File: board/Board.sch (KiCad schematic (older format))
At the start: 56 parts, among them J1 CONN_02X10, J10 CONN_01X03, J11 CONN_01X03, J12 CONN_01X02, J13 CONN_02X09, J14 CONN_02X04, J2 CONN_01X03, J3 CONN_01X03, J4 CONN_01X03, J5 CONN_01X03, J6 CONN_01X03, J7 CONN_01X03, J8 CONN_01X03, J9 CONN_01X03, SW1 SW_Push, SW2 SW_SPDT, SW3 SW_SPDT, U1 STM32F410RBTx, U2 LF33ABDT-TR, U3 ICM-20689, Y1 25 MHz, Y2 32.768 KHz

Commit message: uart signal inverter; battery measurement
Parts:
- removed C3, C4: 1.5pF, Capacitors_SMD:C_0805_HandSoldering, symbol C
- removed R4, R5: 0, Resistors_SMD:R_0805_HandSoldering, symbol R
- removed SW2, SW3: SW_SPDT, Pin_Headers:Pin_Header_Straight_1x03_Pitch2.54mm, symbol SW_SPDT
- removed Y2: 32.768 KHz, Crystals:Crystal_SMD_5032-2pin_5.0x3.2mm_HandSoldering, symbol Crystal
- added J?: CONN_01X01, symbol CONN_01X01
- added J?: GS2, Connectors:GS2, symbol GS2
- added J? (x2): GS3, Connectors:GS3, symbol GS3
- added R?: 62K, symbol R
- added R?: 22K, symbol R
- added U4: SN74LVC1G04, TO_SOT_Packages_SMD:SOT-23-5_HandSoldering, symbol SN74LVC1G04
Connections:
- net labels added: +BATT, BATT_ADC
- net labels removed: +12V
- wire segments 210 -> 206
- no-connect marks 19 -> 20
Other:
- moved on the sheet: J11

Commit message: inverter gate is now optional
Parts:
- added J16: GS3, Connectors:GS3, symbol GS3
- gave numbers to parts that had none: 6
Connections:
- wire segments 206 -> 210
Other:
- moved on the sheet: J11, U4

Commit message: ?
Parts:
- J15, J16, J17: footprint Connectors:GS3 -> Connect:GS3
- J18: footprint Connectors:GS2 -> Connect:GS2
- J19: footprint (none) -> Pin_Headers:Pin_Header_Straight_1x01_Pitch2.54mm
- R4, R5: footprint (none) -> Resistors_SMD:R_0805_HandSoldering
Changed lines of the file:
@@
 F 0 "R4" V 15080 1250 50  0000 C CNN
 F 1 "62K" V 15000 1250 50  0000 C CNN
-F 2 "" V 14930 1250 50  0001 C CNN
+F 2 "Resistors_SMD:R_0805_HandSoldering" V 14930 1250 50  0001 C CNN
 F 3 "" H 15000 1250 50  0001 C CNN
 	1    15000 1250
@@
 F 0 "R5" V 15080 1650 50  0000 C CNN
 F 1 "22K" V 15000 1650 50  0000 C CNN
-F 2 "" V 14930 1650 50  0001 C CNN
+F 2 "Resistors_SMD:R_0805_HandSoldering" V 14930 1650 50  0001 C CNN
 F 3 "" H 15000 1650 50  0001 C CNN
 	1    15000 1650
@@
 F 0 "J19" H 15350 1050 50  0000 C CNN
 F 1 "CONN_01X01" V 15450 950 50  0000 C CNN
-F 2 "" H 15350 950 50  0001 C CNN
+F 2 "Pin_Headers:Pin_Header_Straight_1x01_Pitch2.54mm" H 15350 950 50  0001 C CNN
 F 3 "" H 15350 950 50  0001 C CNN
 	1    15350 950
@@
 F 0 "J18" V 14800 1100 50  0000 C CNN
 F 1 "GS2" V 14800 801 50  0000 C CNN
-F 2 "Connectors:GS2" V 14774 950 50  0001 C CNN
+F 2 "Connect:GS2" V 14774 950 50  0001 C CNN
 F 3 "" H 14700 950 50  0001 C CNN
 	1    14700 950
@@
 F 0 "J15" H 1200 2600 50  0000 C CNN
 F 1 "GS3" H 1200 2201 50  0000 C CNN
-F 2 "Connectors:GS3" V 1238 2326 50  0001 C CNN
+F 2 "Connect:GS3" V 1238 2326 50  0001 C CNN
 F 3 "" H 1150 2400 50  0001 C CNN
 	1    1150 2400
@@
 F 0 "J17" H 10050 4050 50  0000 C CNN
 F 1 "GS3" H 10050 3651 50  0000 C CNN
-F 2 "Connectors:GS3" V 10088 3776 50  0001 C CNN
+F 2 "Connect:GS3" V 10088 3776 50  0001 C CNN
 F 3 "" H 10000 3850 50  0001 C CNN
 	1    10000 3850
@@
 F 0 "J16" H 9600 9250 50  0000 C CNN
 F 1 "GS3" H 9600 8851 50  0000 C CNN
-F 2 "Connectors:GS3" V 9638 8976 50  0001 C CNN
+F 2 "Connect:GS3" V 9638 8976 50  0001 C CNN
 F 3 "" H 9550 9050 50  0001 C CNN
 	1    9550 9050

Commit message: pcb rev2, work in progress
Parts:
- removed J14: CONN_02X04, Pin_Headers:Pin_Header_Straight_2x04_Pitch2.54mm, symbol CONN_02X04
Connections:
- net labels removed: NRF24_CE, NRF24_SPI_CS, NRF24_SPI_MISO, NRF24_SPI_MOSI, NRF24_SPI_SCK
- wire segments 210 -> 196
- no-connect marks 20 -> 24
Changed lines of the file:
@@
 Text GLabel 6150 8350 0    60   Input ~ 0
 PWM_INPUT_4
-$Comp
-L CONN_02X04 J14
-U 1 1 58D8CF93
-P 13500 5750
-F 0 "J14" H 13500 6000 50  0000 C CNN
-F 1 "CONN_02X04" H 13500 5500 50  0000 C CNN
-F 2 "Pin_Headers:Pin_Header_Straight_2x04_Pitch2.54mm" H 13500 4550 50  0001 C CNN
-F 3 "" H 13500 4550 50  0001 C CNN
-	1    13500 5750
-	1    0    0    -1
-$EndComp
-$Comp
-L GND #PWR031
-U 1 1 58D8E88C
-P 13150 6050
-F 0 "#PWR031" H 13150 5800 50  0001 C CNN
-F 1 "GND" H 13150 5900 50  0000 C CNN
-F 2 "" H 13150 6050 50  0001 C CNN
-F 3 "" H 13150 6050 50  0001 C CNN
-	1    13150 6050
-	1    0    0    -1
-$EndComp
-$Comp
-L VCC #PWR032
-U 1 1 58D8FC31
-P 14050 5200
-F 0 "#PWR032" H 14050 5050 50  0001 C CNN
-F 1 "VCC" H 14050 5350 50  0000 C CNN
-F 2 "" H 14050 5200 50  0001 C CNN
-F 3 "" H 14050 5200 50  0001 C CNN
-	1    14050 5200
-	1    0    0    -1
-$EndComp
-NoConn ~ 13750 5900
-Text GLabel 12950 5700 0    60   Input ~ 0
-NRF24_CE
-Text GLabel 14050 5700 2    60   Input ~ 0
-NRF24_SPI_CS
-Text GLabel 11900 5800 0    60   Input ~ 0
-NRF24_SPI_SCK
-Text GLabel 14800 5800 2    60   Input ~ 0
-NRF24_SPI_MOSI
-Text GLabel 12950 5900 0    60   Input ~ 0
-NRF24_SPI_MISO
-Text GLabel 8600 5150 2    60   Input ~ 0
-NRF24_SPI_MOSI
-Text GLabel 9400 5050 2    60   Input ~ 0
-NRF24_SPI_MISO
-Text GLabel 8600 4950 2    60   Input ~ 0
-NRF24_SPI_SCK
-Text GLabel 9400 4850 2    60   Input ~ 0
-NRF24_SPI_CS
-Text GLabel 2450 4250 0    60   Input ~ 0
-NRF24_CE
 Text GLabel 9400 2350 2    60   Input ~ 0
 ICM_SPI_CS
@@
 $EndComp
 $Comp
-L GND #PWR033
+L GND #PWR031
 U 1 1 58DA392C
 P 13700 1800
-F 0 "#PWR033" H 13700 1550 50  0001 C CNN
+F 0 "#PWR031" H 13700 1550 50  0001 C CNN
 F 1 "GND" H 13700 1650 50  0000 C CNN
 F 2 "" H 13700 1800 50  0001 C CNN
@@
 $EndComp
 $Comp
-L GND #PWR034
+L GND #PWR032
 U 1 1 58DA6641
 P 1500 4750
-F 0 "#PWR034" H 1500 4500 50  0001 C CNN
+F 0 "#PWR032" H 1500 4500 50  0001 C CNN
 F 1 "GND" H 1500 4600 50  0000 C CNN
 F 2 "" H 1500 4750 50  0001 C CNN
@@
 I2C_SCL
 $Comp
-L GND #PWR035
+L GND #PWR033
 U 1 1 58D99A32
 P 10300 9400
-F 0 "#PWR035" H 10300 9150 50  0001 C CNN
+F 0 "#PWR033" H 10300 9150 50  0001 C CNN
 F 1 "GND" H 10300 9250 50  0000 C CNN
 F 2 "" H 10300 9400 50  0001 C CNN
@@
 $EndComp
 $Comp
-L VCC #PWR036
+L VCC #PWR034
 U 1 1 58D9B26E
 P 9000 6250
-F 0 "#PWR036" H 9000 6100 50  0001 C CNN
+F 0 "#PWR034" H 9000 6100 50  0001 C CNN
 F 1 "VCC" H 9000 6400 50  0000 C CNN
 F 2 "" H 9000 6250 50  0001 C CNN
@@
 PB5
 $Comp
-L GND #PWR037
+L GND #PWR035
 U 1 1 58DAF3FA
 P 12050 7900
-F 0 "#PWR037" H 12050 7650 50  0001 C CNN
+F 0 "#PWR035" H 12050 7650 50  0001 C CNN
 F 1 "GND" H 12050 7750 50  0000 C CNN
 F 2 "" H 12050 7900 50  0001 C CNN
@@
 $EndComp
 $Comp
-L PWR_FLAG #FLG038
+L PWR_FLAG #FLG036
 U 1 1 58DB2A85
 P 11150 1500
-F 0 "#FLG038" H 11150 1575 50  0001 C CNN
+F 0 "#FLG036" H 11150 1575 50  0001 C CNN
 F 1 "PWR_FLAG" H 10950 1650 50  0000 C CNN
 F 2 "" H 11150 1500 50  0001 C CNN
@@
 $EndComp
 $Comp
-L PWR_FLAG #FLG039
+L PWR_FLAG #FLG037
 U 1 1 58DB1674
 P 11250 1000
-F 0 "#FLG039" H 11250 1075 50  0001 C CNN
+F 0 "#FLG037" H 11250 1075 50  0001 C CNN
 F 1 "PWR_FLAG" H 11250 1150 50  0000 C CNN
 F 2 "" H 11250 1000 50  0001 C CNN
@@
 $EndComp
 $Comp
-L GND #PWR040
+L GND #PWR038
 U 1 1 58DB0976
 P 6550 8900
-F 0 "#PWR040" H 6550 8650 50  0001 C CNN
+F 0 "#PWR038" H 6550 8650 50  0001 C CNN
 F 1 "GND" H 6550 8750 50  0000 C CNN
 F 2 "" H 6550 8900 50  0001 C CNN
@@
 $EndComp
 $Comp
-L VCC #PWR041
+L VCC #PWR039
 U 1 1 58F60FBC
 P 8400 9250
-F 0 "#PWR041" H 8400 9100 50  0001 C CNN
+F 0 "#PWR039" H 8400 9100 50  0001 C CNN
 F 1 "VCC" H 8400 9400 50  0000 C CNN
 F 2 "" H 8400 9250 50  0001 C CNN
@@
 $EndComp
 $Comp
-L GND #PWR042
+L GND #PWR040
 U 1 1 58F61042
 P 8400 9850
-F 0 "#PWR042" H 8400 9600 50  0001 C CNN
+F 0 "#PWR040" H 8400 9600 50  0001 C CNN
 F 1 "GND" H 8400 9700 50  0000 C CNN
 F 2 "" H 8400 9850 50  0001 C CNN
@@
 $EndComp
 $Comp
-L GND #PWR043
+L GND #PWR041
 U 1 1 58F6AF97
 P 15000 1900
-F 0 "#PWR043" H 15000 1650 50  0001 C CNN
+F 0 "#PWR041" H 15000 1650 50  0001 C CNN
 F 1 "GND" H 15000 1750 50  0000 C CNN
 F 2 "" H 15000 1900 50  0001 C CNN
@@
 $EndComp
 $Comp
-L +BATT #PWR044
+L +BATT #PWR042
 U 1 1 58F72A6D
 P 11550 1000
-F 0 "#PWR044" H 11550 850 50  0001 C CNN
+F 0 "#PWR042" H 11550 850 50  0001 C CNN
 F 1 "+BATT" H 11550 1140 50  0000 C CNN
 F 2 "" H 11550 1000 50  0001 C CNN
@@
 $EndComp
 $Comp
-L +BATT #PWR045
+L +BATT #PWR043
 U 1 1 58F73262
 P 14400 800
-F 0 "#PWR045" H 14400 650 50  0001 C CNN
+F 0 "#PWR043" H 14400 650 50  0001 C CNN
 F 1 "+BATT" H 14400 940 50  0000 C CNN
 F 2 "" H 14400 800 50  0001 C CNN
@@
 Wire Wire Line
 	6700 6900 6550 6900
-Wire Wire Line
-	13750 5600 14050 5600
-Wire Wire Line
-	14050 5600 14050 5200
-Wire Wire Line
-	13250 5600 13150 5600
-Wire Wire Line
-	13150 5600 13150 6050
-Wire Wire Line
-	13250 5700 12950 5700
-Wire Wire Line
-	13750 5700 14050 5700
-Wire Wire Line
-	11900 5800 13250 5800
-Wire Wire Line
-	13750 5800 14800 5800
-Wire Wire Line
-	13250 5900 12950 5900
-Wire Wire Line
-	8200 5150 8600 5150
-Wire Wire Line
-	9400 5050 8200 5050
-Wire Wire Line
-	8600 4950 8200 4950
-Wire Wire Line
-	9400 4850 8200 4850
-Wire Wire Line
-	2450 4250 2800 4250
 Wire Wire Line
 	8200 2350 9400 2350
@@
 Wire Wire Line
 	9050 9150 9400 9150
+NoConn ~ 2800 4250
+NoConn ~ 8200 4850
+NoConn ~ 8200 4950
+NoConn ~ 8200 5050
+NoConn ~ 8200 5150
 $EndSCHEMATC

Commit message: removed GPIO headers
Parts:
- removed J13: CONN_02X09, Pin_Headers:Pin_Header_Straight_2x09_Pitch2.54mm, symbol CONN_02X09
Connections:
- net labels removed: PA12, PB11, PB5, PC1, PC11, PC12, PC13, PC2, PC3, PC7, PC8, PC9
- wire segments 196 -> 183
- no-connect marks 24 -> 31
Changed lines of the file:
@@
 	1    0    0    -1
 $EndComp
-Text GLabel 8500 4750 2    60   Input ~ 0
-PB11
-Text GLabel 11100 7300 0    60   Input ~ 0
-PB11
-Text GLabel 2800 3750 0    60   Input ~ 0
-PC1
-Text GLabel 2550 3850 0    60   Input ~ 0
-PC2
-Text GLabel 2800 3950 0    60   Input ~ 0
-PC3
-Text GLabel 11100 7500 0    60   Input ~ 0
-PC1
-Text GLabel 11400 7600 0    60   Input ~ 0
-PC2
-Text GLabel 11100 7700 0    60   Input ~ 0
-PC3
-Text GLabel 2800 4350 0    60   Input ~ 0
-PC7
-Text GLabel 2500 4450 0    60   Input ~ 0
-PC8
-Text GLabel 2800 4550 0    60   Input ~ 0
-PC9
-Text GLabel 2800 4750 0    60   Input ~ 0
-PC11
-Text GLabel 2500 4850 0    60   Input ~ 0
-PC12
-Text GLabel 2800 4950 0    60   Input ~ 0
-PC13
-Text GLabel 11400 7800 0    60   Input ~ 0
-PC7
-Text GLabel 11900 7000 2    60   Input ~ 0
-PC8
-Text GLabel 12250 7300 2    60   Input ~ 0
-PC11
-Text GLabel 12250 7100 2    60   Input ~ 0
-PC9
-Text GLabel 11900 7400 2    60   Input ~ 0
-PC12
-Text GLabel 12250 7500 2    60   Input ~ 0
-PC13
-Text GLabel 8200 4150 2    60   Input ~ 0
-PB5
-Text GLabel 8200 3150 2    60   Input ~ 0
-PA12
-Text GLabel 12250 7700 2    60   Input ~ 0
-PA12
-Text GLabel 11900 7600 2    60   Input ~ 0
-PB5
-$Comp
-L GND #PWR035
-U 1 1 58DAF3FA
-P 12050 7900
-F 0 "#PWR035" H 12050 7650 50  0001 C CNN
-F 1 "GND" H 12050 7750 50  0000 C CNN
-F 2 "" H 12050 7900 50  0001 C CNN
-F 3 "" H 12050 7900 50  0001 C CNN
-	1    12050 7900
-	1    0    0    -1
-$EndComp
-$Comp
-L PWR_FLAG #FLG036
+$Comp
+L PWR_FLAG #FLG035
 U 1 1 58DB2A85
 P 11150 1500
-F 0 "#FLG036" H 11150 1575 50  0001 C CNN
+F 0 "#FLG035" H 11150 1575 50  0001 C CNN
 F 1 "PWR_FLAG" H 10950 1650 50  0000 C CNN
 F 2 "" H 11150 1500 50  0001 C CNN
@@
 $EndComp
 $Comp
-L PWR_FLAG #FLG037
+L PWR_FLAG #FLG036
 U 1 1 58DB1674
 P 11250 1000
-F 0 "#FLG037" H 11250 1075 50  0001 C CNN
+F 0 "#FLG036" H 11250 1075 50  0001 C CNN
 F 1 "PWR_FLAG" H 11250 1150 50  0000 C CNN
 F 2 "" H 11250 1000 50  0001 C CNN
@@
 $EndComp
 $Comp
-L GND #PWR038
+L GND #PWR037
 U 1 1 58DB0976
 P 6550 8900
-F 0 "#PWR038" H 6550 8650 50  0001 C CNN
+F 0 "#PWR037" H 6550 8650 50  0001 C CNN
 F 1 "GND" H 6550 8750 50  0000 C CNN
 F 2 "" H 6550 8900 50  0001 C CNN
@@
 NoConn ~ 8200 3750
 NoConn ~ 8200 3650
-NoConn ~ 11400 7200
-NoConn ~ 11400 7100
-NoConn ~ 11400 7000
-NoConn ~ 11400 7400
 NoConn ~ 2800 4650
-$Comp
-L CONN_02X09 J13
-U 1 1 58DA29EE
-P 11650 7400
-F 0 "J13" H 11650 7900 50  0000 C CNN
-F 1 "CONN_02X09" V 11650 7400 50  0000 C CNN
-F 2 "Pin_Headers:Pin_Header_Straight_2x09_Pitch2.54mm" H 11650 6200 50  0001 C CNN
-F 3 "" H 11650 6200 50  0001 C CNN
-	1    11650 7400
-	1    0    0    -1
-$EndComp
-NoConn ~ 11900 7200
 $Comp
 L SN74LVC1G04 U4
@@
 $EndComp
 $Comp
-L VCC #PWR039
+L VCC #PWR038
 U 1 1 58F60FBC
 P 8400 9250
-F 0 "#PWR039" H 8400 9100 50  0001 C CNN
+F 0 "#PWR038" H 8400 9100 50  0001 C CNN
 F 1 "VCC" H 8400 9400 50  0000 C CNN
 F 2 "" H 8400 9250 50  0001 C CNN
@@
 $EndComp
 $Comp
-L GND #PWR040
+L GND #PWR039
 U 1 1 58F61042
 P 8400 9850
-F 0 "#PWR040" H 8400 9600 50  0001 C CNN
+F 0 "#PWR039" H 8400 9600 50  0001 C CNN
 F 1 "GND" H 8400 9700 50  0000 C CNN
 F 2 "" H 8400 9850 50  0001 C CNN
@@
 $EndComp
 $Comp
-L GND #PWR041
+L GND #PWR040
 U 1 1 58F6AF97
 P 15000 1900
-F 0 "#PWR041" H 15000 1650 50  0001 C CNN
+F 0 "#PWR040" H 15000 1650 50  0001 C CNN
 F 1 "GND" H 15000 1750 50  0000 C CNN
 F 2 "" H 15000 1900 50  0001 C CNN
@@
 $EndComp
 $Comp
-L +BATT #PWR042
+L +BATT #PWR041
 U 1 1 58F72A6D
 P 11550 1000
-F 0 "#PWR042" H 11550 850 50  0001 C CNN
+F 0 "#PWR041" H 11550 850 50  0001 C CNN
 F 1 "+BATT" H 11550 1140 50  0000 C CNN
 F 2 "" H 11550 1000 50  0001 C CNN
@@
 $EndComp
 $Comp
-L +BATT #PWR043
+L +BATT #PWR042
 U 1 1 58F73262
 P 14400 800
-F 0 "#PWR043" H 14400 650 50  0001 C CNN
+F 0 "#PWR042" H 14400 650 50  0001 C CNN
 F 1 "+BATT" H 14400 940 50  0000 C CNN
 F 2 "" H 14400 800 50  0001 C CNN
@@
 Connection ~ 4150 8550
 Wire Wire Line
-	4300 8550 4150 8550
+	4150 8550 4300 8550
 Connection ~ 4150 8000
 Wire Wire Line
-	4300 8000 4150 8000
+	4150 8000 4300 8000
 Connection ~ 4150 7450
 Wire Wire Line
@@
 Connection ~ 1400 1450
 Wire Wire Line
-	1400 1100 1400 1450
-Wire Wire Line
-	1250 1100 1400 1100
+	1400 1450 1400 1100
+Wire Wire Line
+	1400 1100 1250 1100
 Wire Wire Line
 	1300 3850 2050 3850
@@
 	6250 850  6250 700
 Wire Wire Line
-	5700 5550 5700 5650
-Wire Wire Line
-	5700 5650 5300 5650
+	5700 5650 5700 5550
+Wire Wire Line
+	5300 5650 5700 5650
 Wire Wire Line
 	5300 5550 5300 5750
@@
 Connection ~ 6550 8550
 Wire Wire Line
-	6700 8550 6550 8550
+	6550 8550 6700 8550
 Connection ~ 6550 8000
 Wire Wire Line
-	6700 8000 6550 8000
+	6550 8000 6700 8000
 Connection ~ 6550 7450
 Wire Wire Line
@@
 	9050 4250 8200 4250
 Wire Wire Line
-	9250 6750 8500 6750
-Wire Wire Line
-	9250 6850 9000 6850
+	8500 6750 9250 6750
+Wire Wire Line
+	9000 6850 9250 6850
 Wire Wire Line
 	9250 6950 9100 6950
@@
 	9000 6300 9000 6250
 Connection ~ 9000 6300
-Wire Wire Line
-	8200 4750 8500 4750
-Wire Wire Line
-	11400 7300 11100 7300
-Wire Wire Line
-	2550 3850 2800 3850
-Wire Wire Line
-	11100 7500 11400 7500
-Wire Wire Line
-	11400 7700 11100 7700
-Wire Wire Line
-	2500 4450 2800 4450
-Wire Wire Line
-	2500 4850 2800 4850
-Wire Wire Line
-	11900 7100 12250 7100
-Wire Wire Line
-	12250 7300 11900 7300
-Wire Wire Line
-	12250 7500 11900 7500
-Wire Wire Line
-	12250 7700 11900 7700
-Wire Wire Line
-	11900 7800 12050 7800
-Wire Wire Line
-	12050 7800 12050 7900
 Connection ~ 11250 1200
 Wire Wire Line
@@
 	15000 1800 15000 1900
 Wire Wire Line
-	15000 1500 15000 1400
+	15000 1400 15000 1500
 Wire Wire Line
 	15000 950  15000 1100
@@
 NoConn ~ 8200 5050
 NoConn ~ 8200 5150
+NoConn ~ 2800 3750
+NoConn ~ 2800 3850
+NoConn ~ 2800 3950
+NoConn ~ 2800 4350
+NoConn ~ 2800 4450
+NoConn ~ 2800 4550
+NoConn ~ 2800 4750
+NoConn ~ 2800 4850
+NoConn ~ 2800 4950
+NoConn ~ 8200 3150
+NoConn ~ 8200 4750
+NoConn ~ 8200 4150
 $EndSCHEMATC

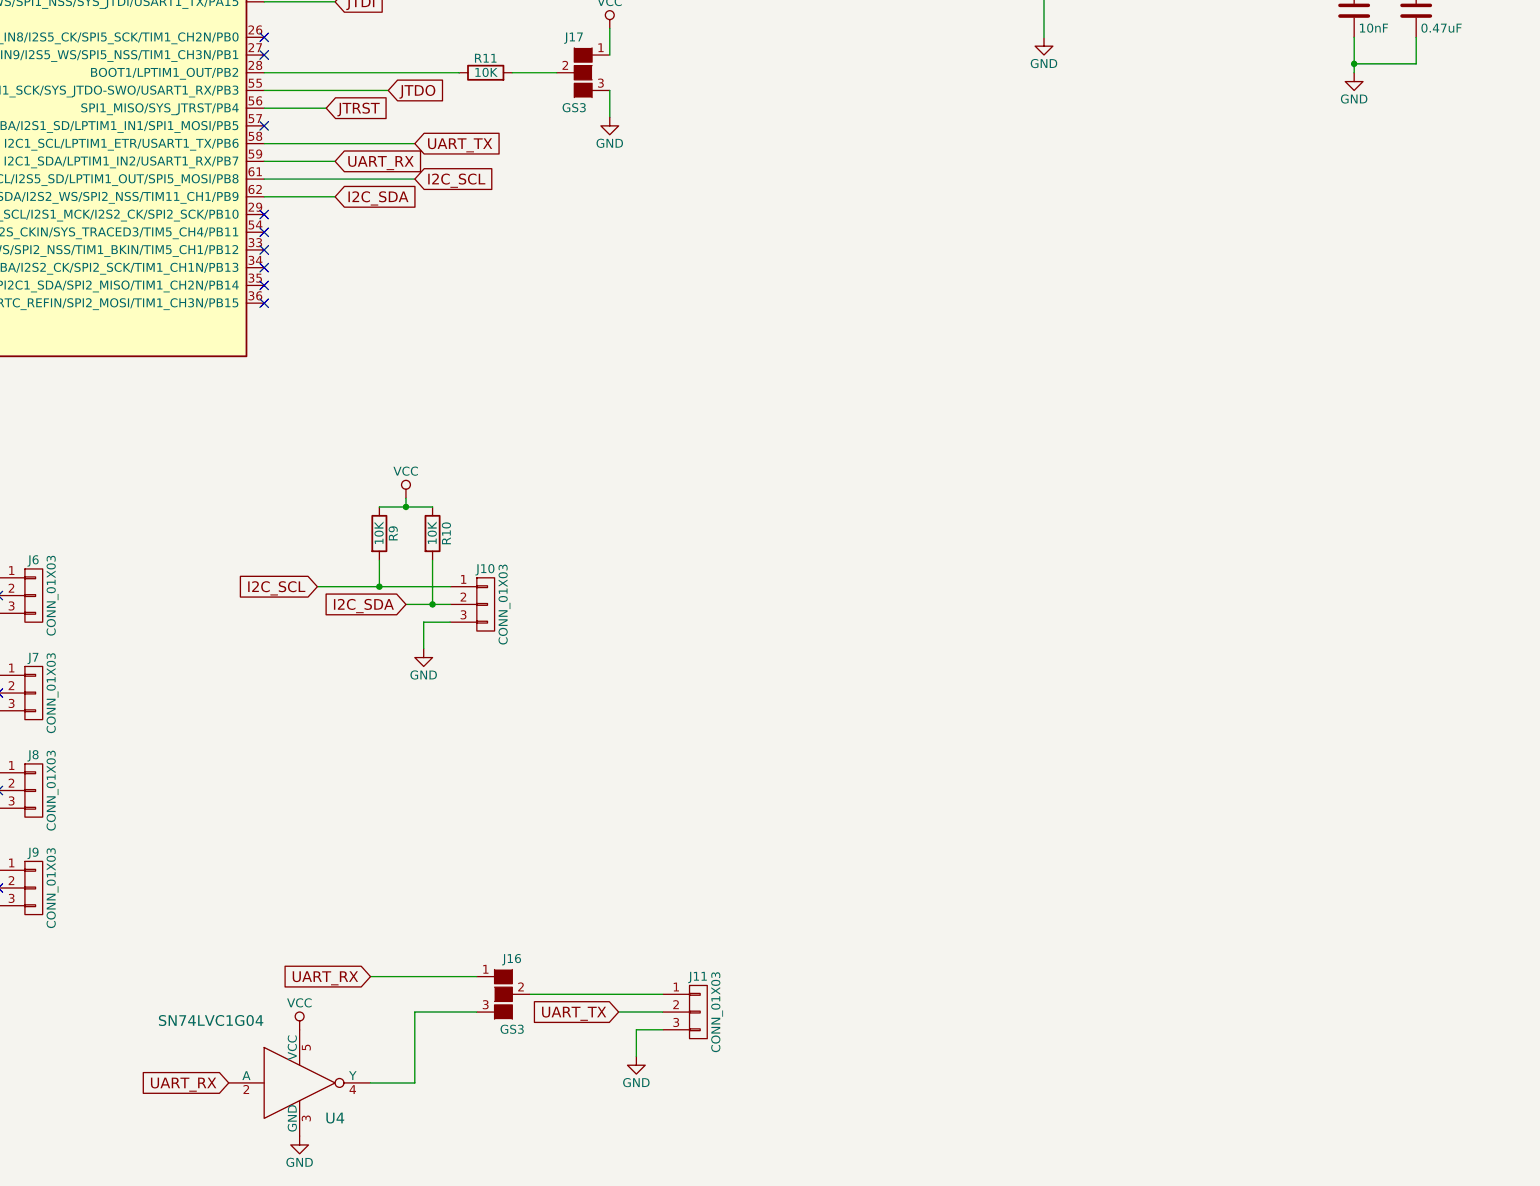
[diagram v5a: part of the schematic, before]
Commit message: added MS5611 component
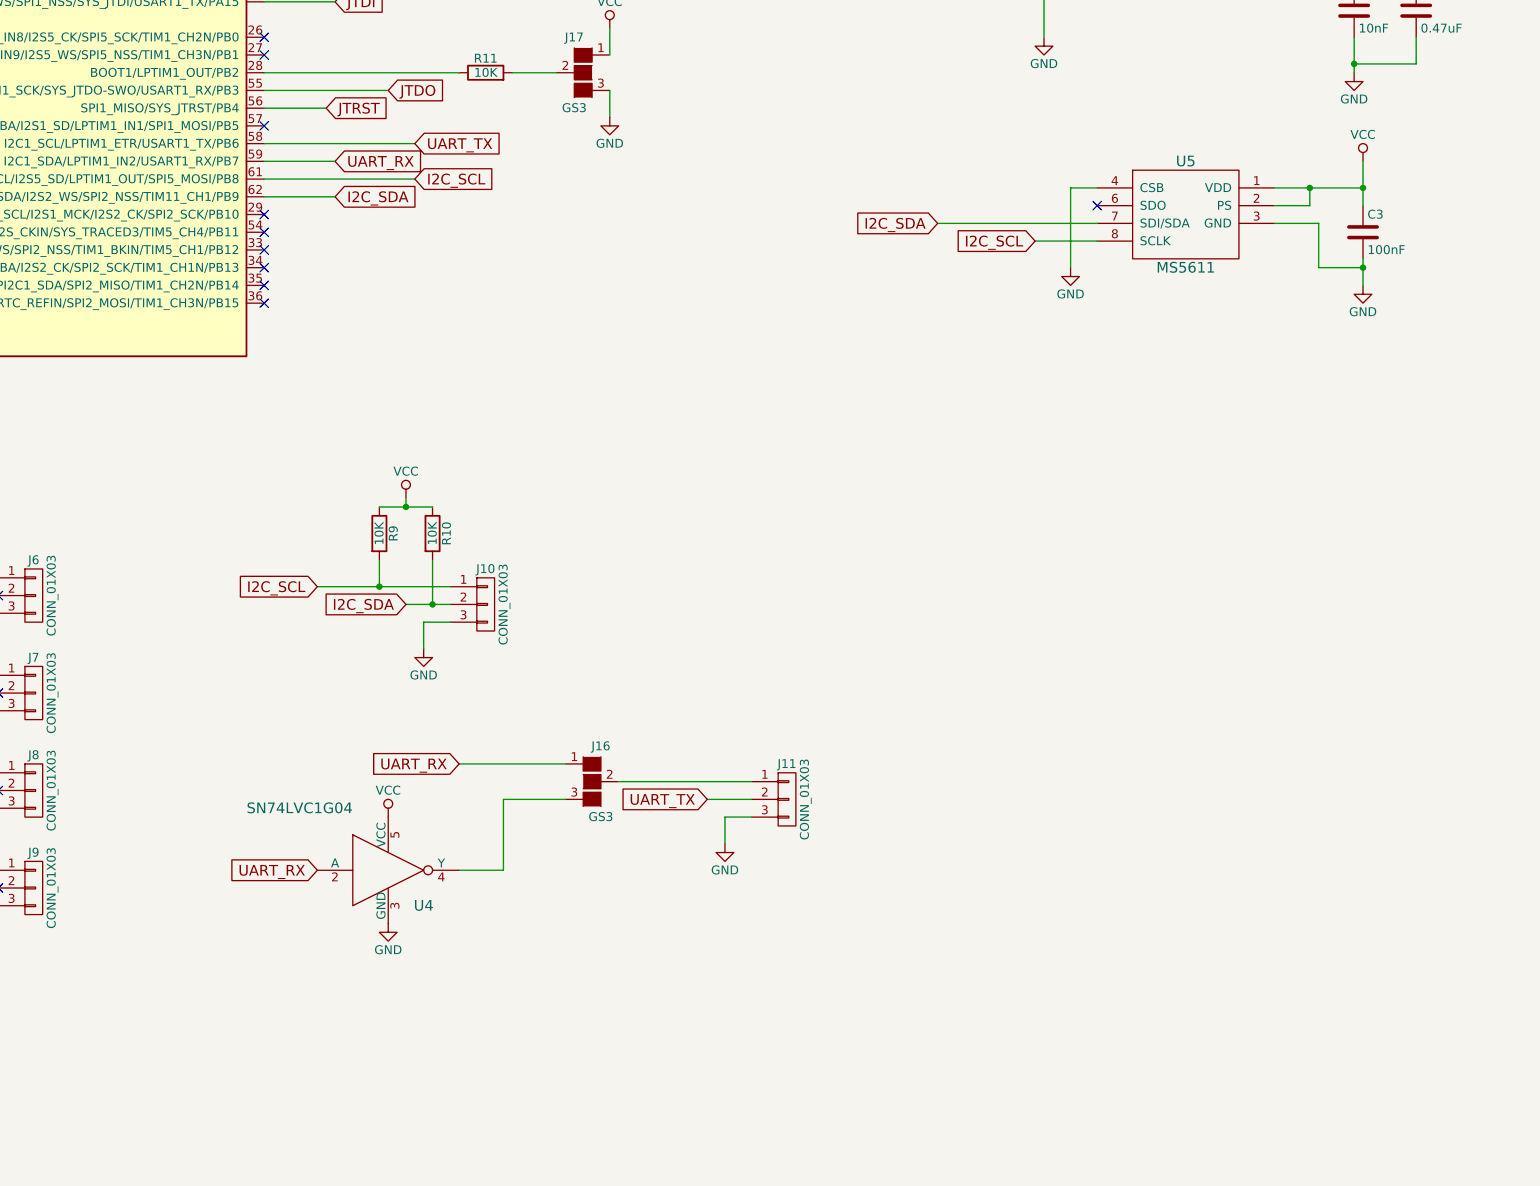
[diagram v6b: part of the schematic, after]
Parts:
- added C3: 100nF, Capacitors_SMD:C_0805_HandSoldering, symbol C
- added U5: MS5611, Local_prints:DFN_5x3_8pin, symbol MS5611
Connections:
- net GND: now also C3.2, U5.3 (GND), U5.4 (CSB)
- net I2C_SCL: now also U5.8 (SCLK)
- net I2C_SDA: now also U5.7 (SDI/SDA)
- net VCC: now also C3.1, U5.1 (VDD), U5.2 (PS)
- no-connect marks 31 -> 32
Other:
- moved on the sheet: J11, J16, U4
